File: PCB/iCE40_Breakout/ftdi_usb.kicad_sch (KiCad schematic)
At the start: 58 parts, among them J5 USB_C_Receptacle_USB2.0_16P, J6 Conn_01x08, Q13 L2N7002SLLT1G, Q14 L2N7002SLLT1G, Q15 L2N7002SLLT1G, Q16 L2N7002SLLT1G, U7 FT2232HPQ, U8 93LC66BT-I/SN, Y1 X3S012000FK1H-HV

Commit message: Changed FT2232 VREGOUT cap to be 10nF, as per datasheet
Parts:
- C39: value 4.7μF -> 10μF; LCSC C23733 -> C15525
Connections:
- net VCCIO/SPI is gone; now on net 3V3: C24.1, C25.1, C26.1, C27.1, C28.1, C29.1, U7.10 (VCCIO), U7.26 (VCCIO), U7.39 (VCCIO), U7.51 (VCCIO), U7.57 (VCC_USB), U7.61 (VCC_PD)
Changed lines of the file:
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@@
+		)
+	)
+	(global_label "3V3"
+		(shape input)
+		(at 271.78 21.59 0)
+		(fields_autoplaced yes)
+		(effects
+			(font
+				(size 1.27 1.27)
+			)
+			(justify left)
+		)
+		(property "Intersheetrefs" "${INTERSHEET_REFS}"
+			(at 278.2728 21.59 0)
+			(effects
+				(font
+					(size 1.27 1.27)
+				)
+				(justify left)
+				(hide yes)
+			)
 		)
 	)
@@
 		(property "Intersheetrefs" "${INTERSHEET_REFS}"
 			(at 61.1028 152.4 0)
-			(effects
-				(font
-					(size 1.27 1.27)
-				)
-				(justify left)
-				(hide yes)
-			)
-		)
-	)
-	(global_label "VCCIO{slash}SPI"
-		(shape input)
-		(at 271.78 21.59 0)
-		(fields_autoplaced yes)
-		(effects
-			(font
-				(size 1.27 1.27)
-			)
-			(justify left)
-		)
-		(property "Intersheetrefs" "${INTERSHEET_REFS}"
-			(at 284.7439 21.59 0)
 			(effects
 				(font
@@
 			)
 		)
-		(property "Value" "4.7μF"
+		(property "Value" "10μF"
 			(at 156.464 38.608 0)
 			(effects
@@
 			)
 		)
-		(property "LCSC" "C23733"
+		(property "LCSC" "C15525"
 			(at 157.48 36.83 0)
 			(effects

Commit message: Changed test points to be SMD pads for size
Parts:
- TP16, TP17, TP18, TP19, TP20: footprint TestPoint:TestPoint_Loop_D1.80mm_Drill1.0mm_Beaded -> TestPoint:TestPoint_Pad_D1.0mm
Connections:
- net VCORE: now reaches C34.1, C35.1, C36.1, C37.1, C38.1, C39.1, TP17.1, U7.25 (VCORE), U7.31 (VREGOUT), U7.44 (VCORE), U7.66 (VCORE), U7.8 (VCORE)
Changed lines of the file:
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@@
 		)
 	)
+	(label "VCORE"
+		(at 162.56 31.75 0)
+		(effects
+			(font
+				(size 1.27 1.27)
+			)
+			(justify left bottom)
+		)
+	)
 	(global_label "USB_CC1"
 		(shape input)
@@
 			)
 		)
-		(property "Footprint" "TestPoint:TestPoint_Loop_D1.80mm_Drill1.0mm_Beaded"
+		(property "Footprint" "TestPoint:TestPoint_Pad_D1.0mm"
 			(at 55.88 22.86 0)
 			(effects
@@
 			)
 		)
-		(property "Footprint" "TestPoint:TestPoint_Loop_D1.80mm_Drill1.0mm_Beaded"
+		(property "Footprint" "TestPoint:TestPoint_Pad_D1.0mm"
 			(at 139.7 105.41 0)
 			(effects
@@
 			)
 		)
-		(property "Footprint" "TestPoint:TestPoint_Loop_D1.80mm_Drill1.0mm_Beaded"
+		(property "Footprint" "TestPoint:TestPoint_Pad_D1.0mm"
 			(at 132.08 105.41 0)
 			(effects
@@
 			)
 		)
-		(property "Footprint" "TestPoint:TestPoint_Loop_D1.80mm_Drill1.0mm_Beaded"
+		(property "Footprint" "TestPoint:TestPoint_Pad_D1.0mm"
 			(at 166.37 29.21 0)
 			(effects
@@
 			)
 		)
-		(property "Footprint" "TestPoint:TestPoint_Loop_D1.80mm_Drill1.0mm_Beaded"
+		(property "Footprint" "TestPoint:TestPoint_Pad_D1.0mm"
 			(at 124.46 105.41 0)
 			(effects

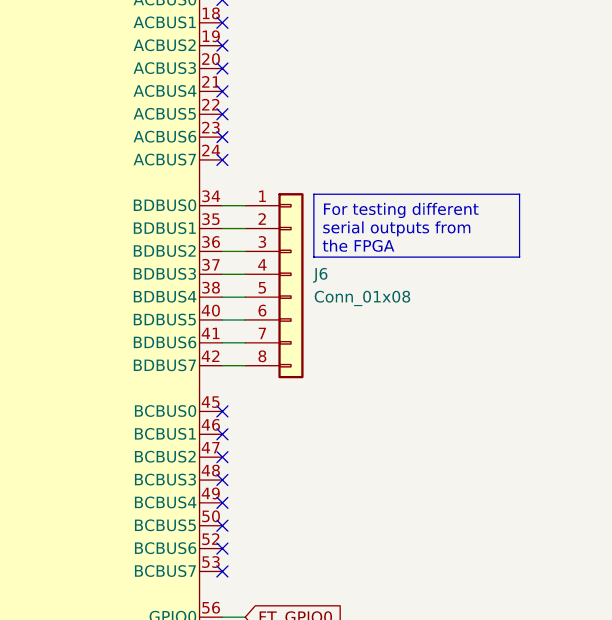
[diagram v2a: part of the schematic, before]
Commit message: Added GND and 3V3 to FTDI port B
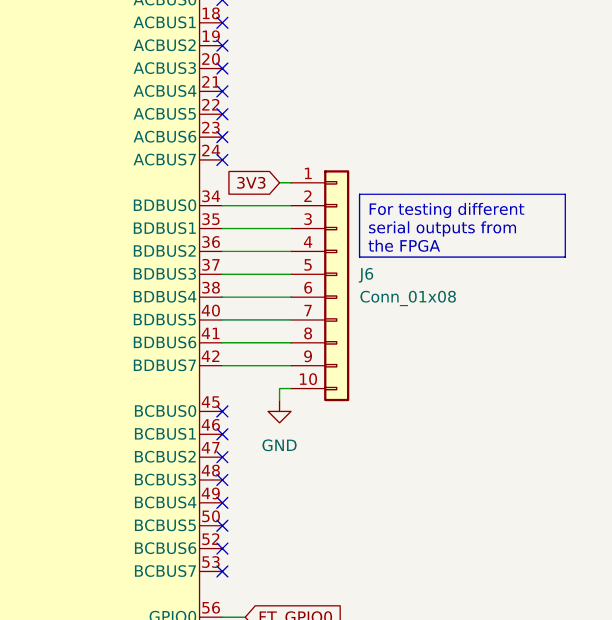
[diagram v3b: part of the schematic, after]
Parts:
- J6: footprint Connector_PinSocket_2.54mm:PinSocket_1x08_P2.54mm_Vertical -> Connector_PinSocket_2.54mm:PinSocket_1x10_P2.54mm_Vertical; symbol Connector_Generic:Conn_01x08 -> Connector_Generic:Conn_01x10
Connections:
- net 3V3: now also J6.1 (Pin_1)
- net GND: now also J6.10 (Pin_10)
- net at U7.34 (BDBUS0): now also J6.2 (Pin_2); no longer J6.1 (Pin_1)
- net at U7.35 (BDBUS1): now also J6.3 (Pin_3); no longer J6.2 (Pin_2)
- net at U7.36 (BDBUS2): now also J6.4 (Pin_4); no longer J6.3 (Pin_3)
- net at U7.37 (BDBUS3): now also J6.5 (Pin_5); no longer J6.4 (Pin_4)
- net at U7.38 (BDBUS4): now also J6.6 (Pin_6); no longer J6.5 (Pin_5)
- net at U7.40 (BDBUS5): now also J6.7 (Pin_7); no longer J6.6 (Pin_6)
- net at U7.41 (BDBUS6): now also J6.8 (Pin_8); no longer J6.7 (Pin_7)
- net at U7.42 (BDBUS7): now also J6.9 (Pin_9); no longer J6.8 (Pin_8)
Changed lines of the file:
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@@
 	(text_box "For testing different serial outputs from the FPGA"
 		(exclude_from_sim no)
-		(at 252.73 88.9 0)
+		(at 257.81 88.9 0)
 		(size 22.86 6.985)
 		(margins 0.9525 0.9525 0.9525 0.9525)
@@
 	(wire
 		(pts
-			(xy 242.57 100.33) (xy 245.11 100.33)
+			(xy 242.57 100.33) (xy 250.19 100.33)
 		)
 		(stroke
@@
 	(wire
 		(pts
+			(xy 248.92 110.49) (xy 250.19 110.49)
+		)
+		(stroke
+			(width 0)
+			(type default)
+		)
+	)
+	(wire
+		(pts
 			(xy 193.04 158.75) (xy 193.04 156.21)
 		)
@@
 	(wire
 		(pts
-			(xy 242.57 95.25) (xy 245.11 95.25)
+			(xy 242.57 95.25) (xy 250.19 95.25)
 		)
 		(stroke
@@
 	(wire
 		(pts
-			(xy 242.57 97.79) (xy 245.11 97.79)
+			(xy 242.57 97.79) (xy 250.19 97.79)
 		)
 		(stroke
@@
 	(wire
 		(pts
-			(xy 242.57 107.95) (xy 245.11 107.95)
+			(xy 242.57 107.95) (xy 250.19 107.95)
 		)
 		(stroke
@@
 	(wire
 		(pts
-			(xy 242.57 92.71) (xy 245.11 92.71)
+			(xy 242.57 92.71) (xy 250.19 92.71)
 		)
 		(stroke
@@
 	(wire
 		(pts
+			(xy 248.92 87.63) (xy 250.19 87.63)
+		)
+		(stroke
+			(width 0)
+			(type default)
+		)
+	)
+	(wire
+		(pts
 			(xy 176.53 100.33) (xy 179.07 100.33)
 		)
@@
 	(wire
 		(pts
-			(xy 242.57 102.87) (xy 245.11 102.87)
+			(xy 242.57 102.87) (xy 250.19 102.87)
 		)
 		(stroke
@@
 	(wire
 		(pts
-			(xy 242.57 105.41) (xy 245.11 105.41)
+			(xy 242.57 105.41) (xy 250.19 105.41)
 		)
 		(stroke
@@
 	(wire
 		(pts
-			(xy 242.57 90.17) (xy 245.11 90.17)
+			(xy 242.57 90.17) (xy 250.19 90.17)
 		)
 		(stroke
@@
 		)
 	)
+	(wire
+		(pts
+			(xy 248.92 111.76) (xy 248.92 110.49)
+		)
+		(stroke
+			(width 0)
+			(type default)
+		)
+	)
 	(label "VCORE"
 		(at 162.56 31.75 0)
@@
 		)
 	)
+	(global_label "3V3"
+		(shape input)
+		(at 248.92 87.63 180)
+		(fields_autoplaced yes)
+		(effects
+			(font
+				(size 1.27 1.27)
+			)
+			(justify right)
+		)
+		(property "Intersheetrefs" "${INTERSHEET_REFS}"
+			(at 242.4272 87.63 0)
+			(effects
+				(font
+					(size 1.27 1.27)
+				)
+				(justify right)
+				(hide yes)
+			)
+		)
+	)
 	(global_label "USB_SVBUS"
 		(shape input)
@@
 	)
 	(symbol
-		(lib_id "Connector_Generic:Conn_01x08")
-		(at 250.19 97.79 0)
+		(lib_id "Connector_Generic:Conn_01x10")
+		(at 255.27 97.79 0)
 		(unit 1)
 		(exclude_from_sim no)
@@
 		(fields_autoplaced yes)
 		(property "Reference" "J6"
-			(at 252.73 97.7899 0)
+			(at 257.81 97.7899 0)
 			(effects
 				(font
@@
 		)
 		(property "Value" "Conn_01x08"
-			(at 252.73 100.3299 0)
+			(at 257.81 100.3299 0)
 			(effects
 				(font
@@
 			)
 		)
-		(property "Footprint" "Connector_PinSocket_2.54mm:PinSocket_1x08_P2.54mm_Vertical"
-			(at 250.19 97.79 0)
+		(property "Footprint" "Connector_PinSocket_2.54mm:PinSocket_1x10_P2.54mm_Vertical"
+			(at 255.27 97.79 0)
 			(effects
 				(font
@@
 		)
 		(property "Datasheet" "~"
-			(at 250.19 97.79 0)
+			(at 255.27 97.79 0)
 			(effects
 				(font
@@
 			)
 		)
-		(property "Description" "Generic connector, single row, 01x08, script generated (kicad-library-utils/schlib/autogen/connector/)"
-			(at 250.19 97.79 0)
+		(property "Description" "Generic connector, single row, 01x10, script generated (kicad-library-utils/schlib/autogen/connector/)"
+			(at 255.27 97.79 0)
 			(effects
 				(font
@@
 		(pin "2"
 		)
+		(pin "10"
+		)
+		(pin "9"
+		)
 		(instances
 			(project "iCE40_Breakout"
@@
 					(unit 1)
 				)
+			)
+		)
+	)
+	(symbol
+		(lib_id "power:GND")
+		(at 248.92 111.76 0)
+		(unit 1)
+		(exclude_from_sim no)
+		(in_bom yes)
+		(on_board yes)
+		(dnp no)
+		(property "Reference" "#PWR057"
+			(at 248.92 118.11 0)
+			(effects
+				(font
+					(size 1.27 1.27)
+				)
+				(hide yes)
+			)
+		)
+		(property "Value" "GND"
+			(at 248.92 116.84 0)
+			(effects
+				(font
+					(size 1.27 1.27)
+				)
+			)
+		)
+		(property "Footprint" ""
+			(at 248.92 111.76 0)
+			(effects
+				(font
+					(size 1.27 1.27)
+				)
+				(hide yes)
+			)
+		)
+		(property "Datasheet" ""
+			(at 248.92 111.76 0)
+			(effects
+				(font
+					(size 1.27 1.27)
+				)
+				(hide yes)
+			)
+		)
+		(property "Description" "Power symbol creates a global label with name \"GND\" , ground"
+			(at 248.92 111.76 0)
+			(effects
+				(font
+					(size 1.27 1.27)
+				)
+				(hide yes)
+			)
+		)
+		(pin "1"
+		)
+		(instances
+			(project "iCE40_Breakout"
+				(path "/ce4d7974-ef38-4eea-8119-381c4298ef02/a0447fef-6cc5-400b-aa41-8540b8ebce1f"
+					(reference "#PWR057")
+					(unit 1)
+				)
